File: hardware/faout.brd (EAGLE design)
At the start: 100 x 70 mm, 147 parts, among them IC2 MT48LC8M16A2, Q1 12MHz, Q2 MUN2214T1, Q3 MUN2214T1, Q4 ASFL, SW1 SMD_TACT_SWITCH, SW2 SMD_TACT_SWITCH, SW3 SMD_TACT_SWITCH, U1 93C46B, U10 ADR435ARZ, U11 AD8627AKSZ-R2, U12 OPA2277UA/2K5E4, U13 OPA2277UA/2K5E4, U14 MCP1700T-2502E/TT, U15 AD7980ARMZ, U16 LM3671MF-3.3, U2 LM3671MF-1.2, U3 FLASH-SPI-25XXSMD1, U4 6SLX9TQG144, U5 AD8220ARMZ, U6 REF102AU, U7 DAC8811DGK, U8 REF102AU, U9 DAC8811DGK

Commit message: Finalize design.
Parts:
- removed R30: 7.47k, faout:R0603
- removed R31: 134k, faout:R0603
- removed R32, R33: 2k, faout:R0603
- added C75: 20pF, faout:R0603
- added C76, C77, C80, C81, C82, C83: 100nF, faout:R0603
- added C78, C79: 1nF, faout:R0603
- added C84, C86: 1uF, faout:R0603
- added C85: 22uF, resistor:C1206
- added JP5: (no value), pinhead:1X06
- added Q5: ASFL, crystal:ASF
- added R10, R11, R12: 100, faout:R0603
- added R9: 4.7k, faout:R0603
- added U17: MCP1700T-2502E/TT, faout:SOT95P264X112-3N
- added U18: AD7980ARMZ, faout:SOP50P490X110-10N
- C1: value 3.3uF -> 10uF; device faout:R0603 -> faout:R0805
- C10, C51, C53, C55, C58, C61: value 100nF -> 4.7uF
- C11, C13, C14, C15, C8, C9: value 100nF -> 10uF; device faout:R0603 -> faout:R0805
- C12: value 4.7uF -> 10uF; device faout:R0603 -> faout:R0805
- C17, C25, C26, C27: value 470nF -> 100nF
- C18, C32, C33, C35, C45: value 470nF -> 4.7uF
- C2: value 18pF -> 10uF; device faout:R0603 -> faout:R0805
- C20, C23, C28, C73: value 4.7uF -> 100nF
- C21, C44: value 10nF -> 4.7uF
- C24: value 10nF -> 100nF
- C29, C30, C40, C41, C42, C48: value 4.7uF -> 470nF
- C3: value 18pF -> 3.3uF
- C37, C39: value 470nF -> 10nF
- C38: value 4.7uF -> 100uF; device faout:R0603 -> rcl:PANASONIC_E
- C4: value 4.7uF -> 18pF
- C5: value 100nF -> 18pF
- C50, C62: value 100nF -> 470nF
- C52, C54: value 1uF? -> 470nF
- C56: value 114pF -> 4.7uF
- C57: value 11.4pF -> 4.7uF
- C59: value 20pF -> 10nF
- C60: value 20pF -> 470nF
- C63, C64: value 1nF -> 4.7uF
- C67: value 100nF -> 1uF?
- C69: value 1uF -> 1uF?
- C70: value 22uF -> 100nF; device resistor:C1206 -> faout:R0603
- C71: value 1uF -> 114pF
- C72: value 4.7uF -> 11.4pF
- C74: value 4.7uF -> 20pF
- JP1: device pinhead:1X02 -> pinhead:1X03
- JP2, JP4: device pinhead:1X06 -> pinhead:1X02
- JP3: device pinhead:1X02 -> pinhead:1X06
- Q1: value 12MHz -> L7912ACV; device faout:TXC_QUARTZ_7A -> faout:TO254P450X1020X1935-3P
- Q2: value MUN2214T1 -> 12MHz; device transistor-npn:SC59-BEC -> faout:TXC_QUARTZ_7A
- Q4: value ASFL -> MUN2214T1; device crystal:ASF -> transistor-npn:SC59-BEC
- R13: value 4.7k -> 100
- R17, R18, R19: value 100 -> 10k
- R20: value 100 -> 300
- R21, R22, R23: value 10k -> 300
- R25, R26: value 300 -> 7.47k
- R27: value 300 -> 134k
- R28: value 300 -> 2k
- R29: value 7.47k -> 2k
- U1: value 93C46B -> 93LC46BT-I/OT; device Bogdan_Commons:SOT23-6 -> faout:SOT95P280X145-6N
- U10: value ADR435ARZ -> DAC8811DGK; device faout:SOIC127P600X175-8N -> faout:MSOP-8
- U11: value AD8627AKSZ-R2 -> REF102AU; device faout:SOT65P210X110-5N -> faout:SOIC127P600X175-8N
- U12: value OPA2277UA/2K5E4 -> DAC8811DGK; device faout:SOIC127P600X175-8N -> faout:MSOP-8
- U13: value OPA2277UA/2K5E4 -> ADR435ARZ
- U14: value MCP1700T-2502E/TT -> AD8627AKSZ-R2; device faout:SOT95P264X112-3N -> faout:SOT65P210X110-5N
- U15: value AD7980ARMZ -> OPA2277UA/2K5E4; device faout:SOP50P490X110-10N -> faout:SOIC127P600X175-8N
- U16: value LM3671MF-3.3 -> OPA2277UA/2K5E4; device faout:SOT95P284X122-5N -> faout:SOIC127P600X175-8N
- U2: value LM3671MF-1.2 -> LM3480IM3-3.3; device faout:SOT95P284X122-5N -> faout:SOT95P251X112-3N
- U3: value FLASH-SPI-25XXSMD1 -> LM2940T-12.0; device GadgetFactory:SO08-EIAJ -> faout:TO254P470X1016X2222-3P
- U4: value 6SLX9TQG144 -> LM3671MF-3.3; device faout:TQ144 -> faout:SOT95P284X122-5N
- U5: value AD8220ARMZ -> LM3671MF-1.2; device faout:SOP65P490X110-8N -> faout:SOT95P284X122-5N
- U6: value REF102AU -> FLASH-SPI-25XXSMD1; device faout:SOIC127P600X175-8N -> GadgetFactory:SO08-EIAJ
- U7: value DAC8811DGK -> 6SLX9TQG144; device faout:MSOP-8 -> faout:TQ144
- U8: value REF102AU -> AD8220ARMZ; device faout:SOIC127P600X175-8N -> faout:SOP65P490X110-8N
- U9: value DAC8811DGK -> REF102AU; device faout:MSOP-8 -> faout:SOIC127P600X175-8N
- moved C74 83.9 mm to (87.9, 30.5), turned to 90 degrees
- moved C12 82.6 mm to (87.3, 61.0)
- moved U16 82.4 mm to (83.2, 31.8), turned to 180 degrees
- moved U5 79.4 mm to (6.03, 54.0), turned to 0 degrees
- moved C73 74.5 mm to (81.3, 43.8), turned to 90 degrees
- moved C72 72.2 mm to (79.4, 52.7)
- moved U2 70.3 mm to (75.6, 63.5), turned to 90 degrees
- moved JP4 64.2 mm to (6.35, 19.4), turned to 180 degrees
- moved JP1 63.5 mm to (95.9, 64.1), turned to 90 degrees
- moved JP3 62.3 mm to (55.9, 57.1), turned to 90 degrees
- moved Q2 60.1 mm to (34.9, 62.5), turned to 180 degrees
- moved U3 57.9 mm to (85.7, 64.8), turned to 0 degrees
- moved C32 56.2 mm to (7.94, 64.5), flipped to the top, turned to 180 degrees
- moved C35 53.2 mm to (7.94, 65.7), flipped to the top
- moved Q4 52.8 mm to (22.5, 2.86), flipped to the top, turned to 90 degrees
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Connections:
- new net +15V: C1.1, JP1.1, U2.2, U3.1
- new net -15V: C2.1, JP1.2, Q1.2
- net !DAC1_CS: now also U10.8, U7.94; no longer U4.94, U7.8
- net !DAC2_CS: now also U12.8, U7.88; no longer U4.88, U9.8
- net !RAM_CAS: now also U7.5; no longer U4.5
- net !RAM_RAS: now also U7.2; no longer U4.2
- net !RAM_WE: now also U7.6; no longer U4.6
- net !USB_OE: now also U7.116; no longer U4.116
- net !USB_RD: now also U7.119; no longer U4.119
- net !USB_RESET: now also JP2.1; no longer JP1.1
- net !USB_RXF: now also U7.121; no longer U4.121
- net !USB_TXE: now also U7.120; no longer U4.120
- net !USB_WR: now also U7.118; no longer U4.118
- net 1V2: now also C33.1, C36.1, C41.1, C43.1, C45.1, C46.1, U5.4, U7.128, U7.19, U7.28, U7.52, U7.89; no longer C26.1, C28.1, C30.1, C31.1, C73.1, C74.1, U2.4, U4.128, U4.19, U4.28, U4.52, U4.89
- net 1V8: now also C20.1, C23.1, C24.1, C3.1; no longer C1.1, C10.1, C11.1, C9.1
- net 2V5: now also C84.1, U17.2, U18.2; no longer C69.1, U14.2, U15.2
- net 3V3: now also C26.1, C28.1, C30.1, C31.1, C38.+, C50.1, C51.1, C52.1, C53.1, C54.1, C55.1, C56.1, C57.1, C58.1, C59.1, C60.1, C61.1, C62.1, C63.1, C64.1, C7.1, JP3.6, JP5.6, Q5.1, Q5.4, R17.2, R18.2, R19.2, R9.2, U5.3, U6.3, U6.7, U6.8, U7.103, U7.122, U7.125, U7.129, U7.135, U7.18, U7.20, U7.31, U7.36, U7.4, U7.42, U7.53, U7.63, U7.69, U7.76, U7.86, U7.90; no longer C13.1, C14.1, C15.1, C16.1, C17.1, C18.1, C19.1, C20.1, C21.1, C23.1, C24.1, C33.1, C36.1, C38.1, C41.1, C43.1, C45.1, C46.1, C5.1, C72.1, JP2.6, JP4.6, Q4.1, Q4.4, R13.2, R21.2, R22.2, R23.2, U16.4, U2.3, U3.3, U3.7, U3.8, U4.103, U4.122, U4.125, U4.129, U4.135, U4.18, U4.20, U4.31, U4.36, U4.42, U4.53, U4.63, U4.69, U4.76, U4.86, U4.90
- net 5V0: now also C18.1, C19.1, C21.1, U4.1, U4.3, U5.1; no longer C12.1, U16.1, U16.3, U2.1
- net A+12V: now also C12.1, C14.1, C73.1, C76.1, C8.1, C80.1, C82.1, U13.2, U14.5, U15.8, U16.8, U3.3, U8.8; no longer C50.1, C58.1, C61.1, C67.1, U10.2, U11.5, U12.8, U13.8, U5.8
- net A+3V3: now also C11.1, C67.1, C68.1, C69.1, C70.1, C86.1, U10.7, U11.2, U12.7, U17.3, U18.10, U2.1, U9.2; no longer C52.1, C53.1, C54.1, C55.1, C71.1, U14.3, U15.10, U6.2, U7.7, U8.2, U9.7
- net A-12V: now also C13.2, C15.2, C77.2, C81.2, C83.2, C9.2, Q1.3, U14.2, U15.4, U16.4, U8.5; no longer C51.2, C62.2, C68.2, U11.2, U12.4, U13.4, U5.5
- net ADC1_CNV: now also U18.6, U7.100; no longer U15.6, U4.100
- net ADC1_REF: now also C85.1, U13.6, U18.1; no longer C70.1, U10.6, U15.1
- net ADC1_SCK: now also U18.8, U7.98; no longer U15.8, U4.98
- net ADC1_SDI: now also U18.9, U7.97; no longer U15.9, U4.97
- net ADC1_SDO: now also U18.7, U7.99; no longer U15.7, U4.99
- net BUTTON1: now also U7.61; no longer U4.61
- net BUTTON2: now also U7.62; no longer U4.62
- net BUTTON3: now also U7.66; no longer U4.66
- net CLK_IN: now also Q5.3, U7.95; no longer Q4.3, U4.95
- net DAC1_CLK: now also U10.1, U7.93; no longer U4.93, U7.1
- net DAC1_IOUT: now also C74.2, U10.5, U16.2; no longer C59.2, U13.2, U7.5
- net DAC1_SDI: now also U10.2, U7.92; no longer U4.92, U7.2
- net DAC1_VOUT: now also C74.1, U10.3, U16.1; no longer C59.1, U13.1, U7.3
- net DAC1_VREF: now also C67.2, C78.2, U10.4, U16.7, U9.4; no longer C52.2, C63.2, U13.7, U6.4, U7.4
- net DAC1_VREFOUT: now also C78.1, R28.2, U16.6; no longer C63.1, R32.2, U13.6
- net DAC2_CLK: now also U12.1, U7.87; no longer U4.87, U9.1
- net DAC2_IOUT: now also C75.2, U12.5, U15.2; no longer C60.2, U12.2, U9.5
- net DAC2_SDI: now also U12.2, U7.85; no longer U4.85, U9.2
- net DAC2_VOUT: now also C75.1, U12.3, U15.1; no longer C60.1, U12.1, U9.3
- net DAC2_VREF: now also C69.2, C79.2, U11.4, U12.4, U15.7; no longer C54.2, C64.2, U12.7, U8.4, U9.4
- net DAC2_VREFOUT: now also C79.1, R29.2, U15.6; no longer C64.1, R33.2, U12.6
- net DISP_A: now also R10.2, U7.55; no longer R14.2, U4.55
- net DISP_B: now also R11.2, U7.56; no longer R15.2, U4.56
- net DISP_C: now also R12.2, U7.48; no longer R16.2, U4.48
- net DISP_CAT1: now also Q4.C; no longer Q3.C
- net DISP_D: now also R13.2, U7.50; no longer R17.2, U4.50
- net DISP_E: now also R14.2, U7.47; no longer R18.2, U4.47
- net DISP_EN1: now also Q4.B, U7.58; no longer Q3.B, U4.58
- net DISP_EN2: now also Q3.B, U7.59; no longer Q2.B, U4.59
- net DISP_F: now also R15.2, U7.51; no longer R19.2, U4.51
- net DISP_G: now also R16.2, U7.57; no longer R20.2, U4.57
- net DISP_INT_A: now also R10.1; no longer R14.1
- net DISP_INT_B: now also R11.1; no longer R15.1
- net DISP_INT_C: now also R12.1; no longer R16.1
- net DISP_INT_D: now also R13.1; no longer R17.1
- net DISP_INT_E: now also R14.1; no longer R18.1
- net DISP_INT_F: now also R15.1; no longer R19.1
- net DISP_INT_G: now also R16.1; no longer R20.1
- net FLASH_CS: now also U6.1, U7.38; no longer U3.1, U4.38
- net FLASH_MISO: now also U6.2, U7.65; no longer U3.2, U4.65
- net FLASH_MOSI: now also U6.5, U7.64; no longer U3.5, U4.64
- net FLASH_SCK: now also U6.6, U7.70; no longer U3.6, U4.70
- net GND: now also C13.1, C15.1, C38.-, C51.2, C52.2, C54.2, C56.2, C59.2, C60.2, C62.2, C63.2, C64.2, C68.2, C76.2, C77.1, C80.2, C81.1, C82.2, C83.1, C84.2, C85.2, C86.2, C9.1, JP1.3, JP2.2, JP3.1, JP4.2, JP5.5, Q1.1, Q4.E, Q5.2, R20.1, R21.1, R22.1, R23.1, U10.6, U12.6, U13.4, U15.3, U16.3, U16.5, U17.1, U18.4, U18.5, U2.3, U3.2, U4.2, U5.2, U6.4, U7.108, U7.113, U7.13, U7.130, U7.136, U7.144, U7.25, U7.3, U7.49, U7.54, U7.60, U7.68, U7.73, U7.77, U7.91, U7.96, U8.6; no longer C13.2, C15.2, C38.2, C51.1, C62.1, C67.2, C68.1, C69.2, C71.2, C74.2, C9.2, JP1.2, JP2.1, JP3.2, JP4.5, Q2.E, Q4.2, R25.1, R27.1, R28.1, R30.1, U10.4, U12.3, U12.5, U13.3, U13.5, U14.1, U15.4, U16.2, U2.2, U3.4, U4.108, U4.113, U4.13, U4.130, U4.136, U4.144, U4.25, U4.3, U4.49, U4.54, U4.60, U4.68, U4.73, U4.77, U4.91, U4.96, U5.6, U7.6, U9.6
- net JP_1: now also JP5.1, U7.84; no longer JP4.1, U4.84
- net JP_2: now also JP5.2, U7.83; no longer JP4.2, U4.83
- net JP_3: now also JP5.3, U7.82; no longer JP4.3, U4.82
- net JP_4: now also JP5.4, U7.81; no longer JP4.4, U4.81
- net LED1: now also U7.80; no longer U4.80
- net LED2: now also U7.79; no longer U4.79
- net LED3: now also U7.78; no longer U4.78
- net LED_4: now also U7.112; no longer U4.112
- net LED_5: now also U7.111; no longer U4.111
- net N$1: now also C4.1, Q2.1; no longer C2.1, Q1.1
- net N$10: now also R28.1, U9.6; no longer R32.1, U6.6
- net N$11: now also U8.1; no longer U5.1
- net N$12: now also C71.1, U14.1, U14.4, U18.3; no longer C56.1, U11.1, U11.4, U15.3
- net N$13: now also R25.2, U8.7; no longer R29.2, U5.7
- net N$14: now also C71.2, R25.1, R26.2, R27.1; no longer C56.2, R29.1, R30.2, R31.1
- net N$15: now also C72.1, R27.2, U14.3; no longer C57.1, R31.2, U11.3
- net N$17: now also Q3.C; no longer Q2.C
- net N$18: now also R17.1; no longer R21.1
- net N$19: now also R18.1; no longer R22.1
- net N$2: now also C5.1, Q2.2; no longer C3.1, Q1.2
- net N$20: now also R19.1; no longer R23.1
- net N$21: now also R20.2; no longer R24.2
- net N$22: now also R21.2; no longer R25.2
- net N$23: now also R22.2; no longer R26.2
- net N$24: now also U4.5; no longer U16.5
- net N$25: now also U5.5; no longer U2.5
- net N$3: now also R23.2; no longer R27.2
- net N$4: now also R24.2; no longer R28.2
- net N$5: now also C16.1, C6.1; no longer C4.1, C7.1
- net N$7: now also C10.1, C17.1; no longer C6.1, C8.1
- net N$8: now also R29.1, U11.6; no longer R33.1, U8.6
- net N$9: now also U8.4; no longer U5.4
- net RAM_A0: now also U7.140; no longer U4.140
- net RAM_A1: now also U7.139; no longer U4.139
- net RAM_A10: now also U7.141; no longer U4.141
- net RAM_A11: now also U7.35; no longer U4.35
- net RAM_A2: now also U7.138; no longer U4.138
- net RAM_A3: now also U7.137; no longer U4.137
- net RAM_A4: now also U7.46; no longer U4.46
- net RAM_A5: now also U7.45; no longer U4.45
- net RAM_A6: now also U7.44; no longer U4.44
- net RAM_A7: now also U7.43; no longer U4.43
- net RAM_A8: now also U7.41; no longer U4.41
- net RAM_A9: now also U7.40; no longer U4.40
- net RAM_BA0: now also U7.143; no longer U4.143
- net RAM_BA1: now also U7.142; no longer U4.142
- net RAM_CKE: now also U7.33; no longer U4.33
- net RAM_CLK: now also U7.32; no longer U4.32
- net RAM_CS: now also U7.1; no longer U4.1
- net RAM_DQ0: now also U7.9; no longer U4.9
- net RAM_DQ1: now also U7.10; no longer U4.10
- net RAM_DQ10: now also U7.23; no longer U4.23
- net RAM_DQ11: now also U7.24; no longer U4.24
- net RAM_DQ12: now also U7.26; no longer U4.26
- net RAM_DQ13: now also U7.27; no longer U4.27
- net RAM_DQ14: now also U7.29; no longer U4.29
- net RAM_DQ15: now also U7.30; no longer U4.30
- net RAM_DQ2: now also U7.11; no longer U4.11
- net RAM_DQ3: now also U7.12; no longer U4.12
- net RAM_DQ4: now also U7.14; no longer U4.14
- net RAM_DQ5: now also U7.15; no longer U4.15
- net RAM_DQ6: now also U7.16; no longer U4.16
- net RAM_DQ7: now also U7.8; no longer U4.8
- net RAM_DQ8: now also U7.21; no longer U4.21
- net RAM_DQ9: now also U7.22; no longer U4.22
- net RAM_DQMH: now also U7.17; no longer U4.17
- net RAM_DQML: now also U7.7; no longer U4.7
- net RESET: now also JP4.1, R9.1, U7.37; no longer JP3.1, R13.1, U4.37
- net TCK: now also JP3.2, U7.109; no longer JP2.2, U4.109
- net TDI: now also JP3.3, U7.110; no longer JP2.3, U4.110
- net TDO: now also JP3.4, U7.106; no longer JP2.4, U4.106
- net TMS: now also JP3.5, U7.107; no longer JP2.5, U4.107
- net USB_CLKOUT: now also U7.123; no longer U4.123
- net USB_D0: now also U7.117; no longer U4.117
- net USB_D1: now also U7.134; no longer U4.134
- net USB_D2: now also U7.133; no longer U4.133
- net USB_D3: now also U7.132; no longer U4.132
- net USB_D4: now also U7.131; no longer U4.131
- net USB_D5: now also U7.127; no longer U4.127
- net USB_D6: now also U7.126; no longer U4.126
- net USB_D7: now also U7.124; no longer U4.124
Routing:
- net 3V3: track 381.6 -> 448.7 mm, vias 38 -> 53
- net 1V2: track 47.0 -> 94.8 mm, vias 5 -> 11
- net USB_V: track 69.8 -> 26.8 mm
- net -15V: track 0.00 -> 36.0 mm
- net +15V: track 0.00 -> 26.0 mm
- net USB_GND: track 26.2 -> 7.79 mm
- net A+3V3: track 121.7 -> 136.4 mm, vias 8 -> 10
- net A-12V: track 85.9 -> 99.8 mm
- net GND: track 6.00 -> 3.14 mm, vias 178 -> 241
- net ADC1_SDI: track 26.2 -> 23.7 mm
- net ADC1_SDO: track 26.2 -> 23.7 mm
- net ADC1_CNV: track 26.2 -> 23.7 mm
- net ADC1_SCK: track 26.2 -> 23.7 mm
- net N$24: track 0.00 -> 2.38 mm
- net N$25: track 0.00 -> 2.38 mm
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- removed copper zone on layer 1, net N$26
- removed copper zone on layer 16, net N$26

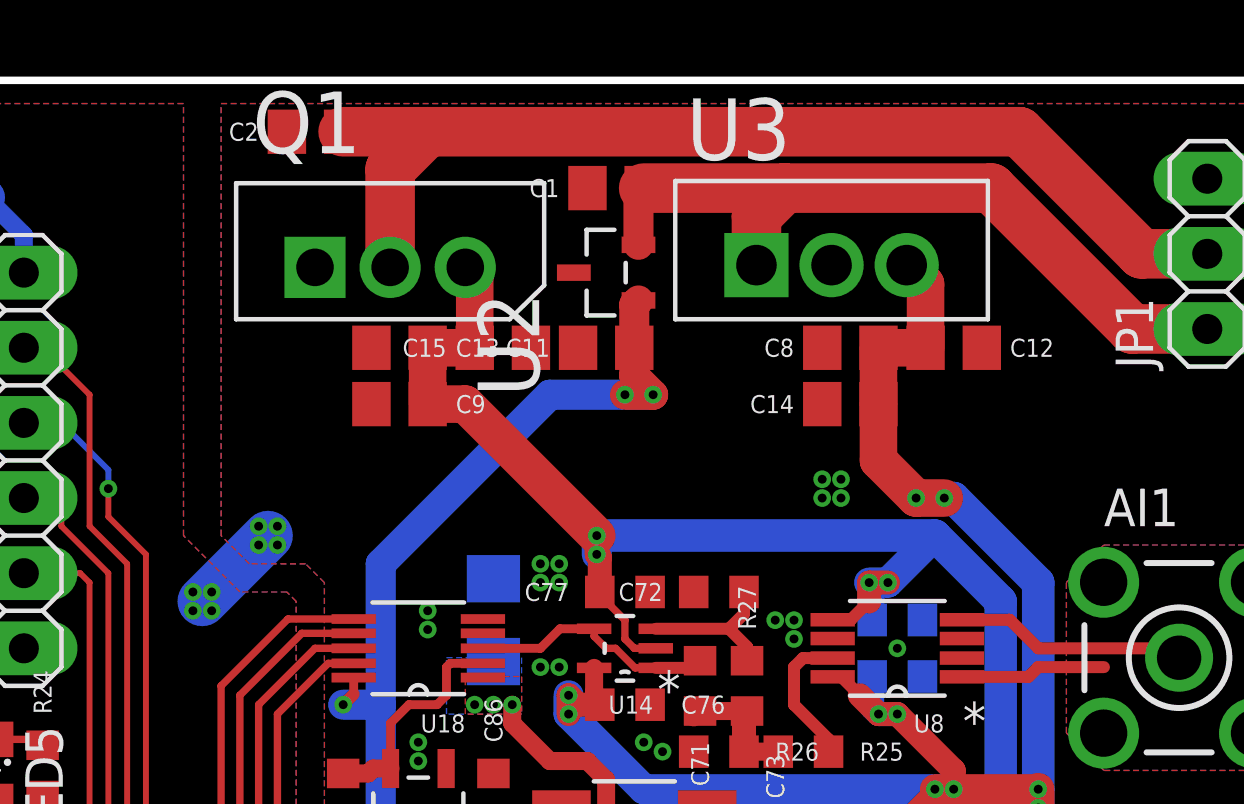
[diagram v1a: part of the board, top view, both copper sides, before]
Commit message: Unify analog regulators.
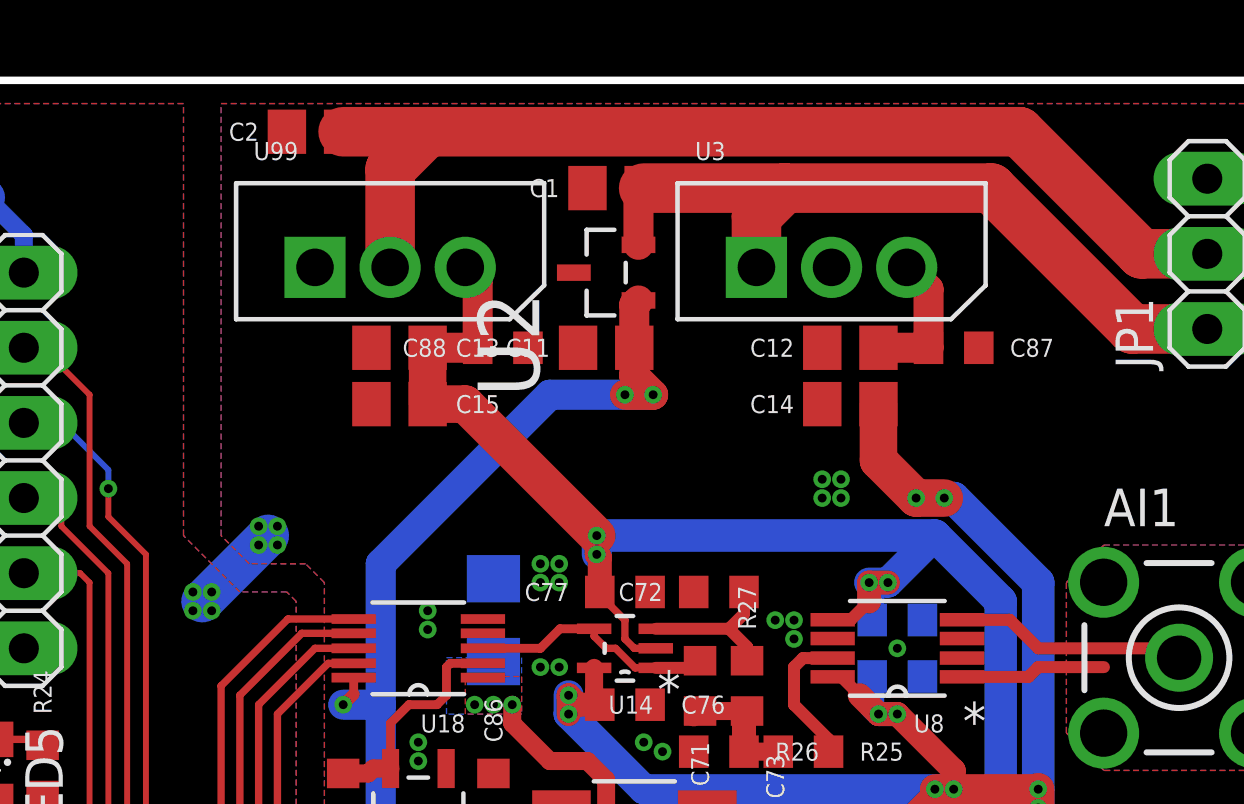
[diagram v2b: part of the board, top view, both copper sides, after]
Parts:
- removed C8, C9: 10uF, faout:R0805
- added C87, C88: 100nF, faout:R0603
- U3: value LM2940T-12.0 -> L7812ACV; device faout:TO254P470X1016X2222-3P -> faout:TO254P450X1020X1935-3P
- moved C15 3.98 mm to (68.6, 59.1), turned to 0 degrees
- moved C12 3.49 mm to (83.8, 61.0), turned to 180 degrees
- renumbered Q1 to U99
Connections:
- net A+12V: now also C87.1; no longer C8.1
- net A-12V: now also C88.2; no longer C9.2
- net GND: now also C87.2, C88.1; no longer C8.2, C9.1
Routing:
- net A+12V: track 123.9 -> 122.1 mm
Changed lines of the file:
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@@
 </element>
 <element name="JP1" library="pinhead" package="1X03" value="" x="95.885" y="64.135" rot="R90"/>
-<element name="U3" library="faout" package="TO254P470X1016X2222-3P" value="LM2940T-12.0" x="85.725" y="64.77">
+<element name="U3" library="faout" package="TO254P450X1020X1935-3P" value="L7812ACV" x="85.725" y="64.77">
 <attribute name="PACKAGE" value="TO-220" x="85.725" y="64.77" size="1.778" layer="27" display="off"/>
-<attribute name="OC_NEWARK" value="41K4614" x="85.725" y="64.77" size="1.778" layer="27" display="off"/>
-<attribute name="MPN" value="LM2940T-12.0" x="85.725" y="64.77" size="1.778" layer="27" display="off"/>
-<attribute name="SUPPLIER" value="NATIONAL SEMICONDUCTOR" x="85.725" y="64.77" size="1.778" layer="27" display="off"/>
-<attribute name="OC_FARNELL" value="9485872" x="85.725" y="64.77" size="1.778" layer="27" display="off"/>
+<attribute name="OC_NEWARK" value="89K0786" x="85.725" y="64.77" size="1.778" layer="27" display="off"/>
+<attribute name="MPN" value="L7812ACV" x="85.725" y="64.77" size="1.778" layer="27" display="off"/>
+<attribute name="SUPPLIER" value="STMicroelectronics" x="85.725" y="64.77" size="1.778" layer="27" display="off"/>
+<attribute name="OC_FARNELL" value="1087091" x="85.725" y="64.77" size="1.778" layer="27" display="off"/>
 </element>
-<element name="Q1" library="faout" package="TO254P450X1020X1935-3P" value="L7912ACV" x="70.8025" y="64.77">
+<element name="U99" library="faout" package="TO254P450X1020X1935-3P" value="L7912ACV" x="70.8025" y="64.77">
 <attribute name="PACKAGE" value="TO-220" x="70.8025" y="64.77" size="1.778" layer="27" display="off"/>
 <attribute name="OC_NEWARK" value="89K0792" x="70.8025" y="64.77" size="1.778" layer="27" display="off"/>
@@
 <attribute name="OC_FARNELL" value="1095391" x="70.8025" y="64.77" size="1.778" layer="27" display="off"/>
 </element>
-<element name="C12" library="faout" package="R0805" value="10uF" x="87.3125" y="60.96">
-<attribute name="OC_FARNELL" value="1867958" x="87.3125" y="60.96" size="1.778" layer="27" display="off"/>
-</element>
-<element name="C8" library="faout" package="R0805" value="10uF" x="83.82" y="60.96" rot="R180">
+<element name="C12" library="faout" package="R0805" value="10uF" x="83.82" y="60.96" rot="R180">
 <attribute name="OC_FARNELL" value="1867958" x="83.82" y="60.96" size="1.778" layer="27" rot="R180" display="off"/>
 </element>
@@
 <attribute name="OC_FARNELL" value="1867958" x="83.82" y="59.055" size="1.778" layer="27" rot="R180" display="off"/>
 </element>
-<element name="C9" library="faout" package="R0805" value="10uF" x="68.58" y="59.055">
-<attribute name="OC_FARNELL" value="1867958" x="68.58" y="59.055" size="1.778" layer="27" display="off"/>
-</element>
 <element name="C13" library="faout" package="R0805" value="10uF" x="68.58" y="60.96">
 <attribute name="OC_FARNELL" value="1867958" x="68.58" y="60.96" size="1.778" layer="27" display="off"/>
 </element>
-<element name="C15" library="faout" package="R0805" value="10uF" x="72.0725" y="60.96" rot="R180">
-<attribute name="OC_FARNELL" value="1867958" x="72.0725" y="60.96" size="1.778" layer="27" rot="R180" display="off"/>
+<element name="C15" library="faout" package="R0805" value="10uF" x="68.58" y="59.055">
+<attribute name="OC_FARNELL" value="1867958" x="68.58" y="59.055" size="1.778" layer="27" display="off"/>
 </element>
 <element name="C1" library="faout" package="R0805" value="10uF" x="75.8825" y="66.3575" rot="R180">
@@
 <attribute name="SUPPLIER" value="Microchip" x="41.5925" y="66.3575" size="1.778" layer="27" display="off"/>
 <attribute name="OC_FARNELL" value="1556164" x="41.5925" y="66.3575" size="1.778" layer="27" display="off"/>
+</element>
+<element name="C87" library="faout" package="R0603" value="100nF" x="87.3125" y="60.96">
+<attribute name="OC_FARNELL" value="1740621" x="87.3125" y="60.96" size="1.778" layer="27" display="off"/>
+</element>
+<element name="C88" library="faout" package="R0603" value="100nF" x="72.0725" y="60.96" rot="R180">
+<attribute name="OC_FARNELL" value="1740621" x="72.0725" y="60.96" size="1.778" layer="27" rot="R180" display="off"/>
 </element>
 </elements>
@@
 <vertex x="62.5475" y="54.61"/>
 </polygon>
-<wire x1="61.9125" y1="52.3875" x2="64.135" y2="54.61" width="1.6764" layer="16"/>
+<wire x1="61.9125" y1="52.3875" x2="64.135" y2="54.61" width="1.4224" layer="16"/>
 <polygon width="0.25" layer="16" rank="6">
 <vertex x="62.5475" y="69.215"/>
@@
 <via x="19.3675" y="35.8775" extent="1-16" drill="0.3"/>
 <contactref element="JP1" pad="3"/>
-<contactref element="Q1" pad="1"/>
+<contactref element="U99" pad="1"/>
 <contactref element="U3" pad="2"/>
 <contactref element="C1" pad="2"/>
 <contactref element="C2" pad="2"/>
-<contactref element="C9" pad="1"/>
-<contactref element="C8" pad="2"/>
 <contactref element="C14" pad="2"/>
 <contactref element="C12" pad="2"/>
@@
 <via x="49.8475" y="67.945" extent="1-16" drill="0.3"/>
 <via x="50.4825" y="67.945" extent="1-16" drill="0.3"/>
+<contactref element="C88" pad="1"/>
+<contactref element="C87" pad="2"/>
 </signal>
 <signal name="USB_DM">
@@
 <contactref element="U3" pad="3"/>
 <contactref element="C12" pad="1"/>
-<contactref element="C8" pad="1"/>
 <contactref element="C14" pad="1"/>
-<wire x1="86.3625" y1="60.96" x2="84.77" y2="60.96" width="1.27" layer="1"/>
-<wire x1="84.77" y1="59.055" x2="84.77" y2="60.96" width="1.27" layer="1"/>
-<wire x1="86.3625" y1="60.96" x2="86.3625" y2="63.1165" width="1.27" layer="1"/>
-<wire x1="86.3625" y1="63.1165" x2="85.725" y2="63.754" width="1.27" layer="1"/>
 <wire x1="84.77" y1="59.055" x2="84.77" y2="57.1525" width="1.27" layer="1"/>
 <wire x1="84.77" y1="57.1525" x2="86.0425" y2="55.88" width="1.27" layer="1"/>
@@
 <via x="86.0425" y="55.88" extent="1-16" drill="0.3"/>
 <via x="86.995" y="55.88" extent="1-16" drill="0.3"/>
+<contactref element="C87" pad="1"/>
+<wire x1="86.4625" y1="60.96" x2="86.4625" y2="62.9403" width="1.016" layer="1"/>
+<wire x1="86.4625" y1="62.9403" x2="85.725" y2="63.6778" width="1.016" layer="1"/>
+<wire x1="86.4625" y1="60.96" x2="84.77" y2="60.96" width="1.016" layer="1"/>
+<wire x1="84.77" y1="59.055" x2="84.77" y2="60.96" width="0" layer="19" extent="1-1"/>
 </signal>
 <signal name="A+3V3">
@@
 <via x="75.2475" y="53.975" extent="1-16" drill="0.3"/>
 <wire x1="75.2475" y1="54.61" x2="75.2475" y2="53.975" width="1.016" layer="16"/>
-<contactref element="Q1" pad="3"/>
-<contactref element="C9" pad="2"/>
 <contactref element="C13" pad="2"/>
 <contactref element="C15" pad="2"/>
+<wire x1="70.8025" y1="59.055" x2="75.2475" y2="54.61" width="1.27" layer="1"/>
+<contactref element="U99" pad="3"/>
+<contactref element="C88" pad="2"/>
+<wire x1="71.2225" y1="60.96" x2="71.2225" y2="63.2578" width="1.016" layer="1"/>
+<wire x1="71.2225" y1="63.2578" x2="70.8025" y2="63.6778" width="1.016" layer="1"/>
+<wire x1="71.2225" y1="60.96" x2="69.53" y2="60.96" width="1.016" layer="1"/>
+<wire x1="70.8025" y1="59.055" x2="69.53" y2="59.055" width="1.27" layer="1"/>
 <wire x1="69.53" y1="59.055" x2="69.53" y2="60.96" width="1.27" layer="1"/>
-<wire x1="69.53" y1="60.96" x2="71.1225" y2="60.96" width="1.27" layer="1"/>
-<wire x1="71.1225" y1="60.96" x2="71.1225" y2="63.3578" width="1.27" layer="1"/>
-<wire x1="71.1225" y1="63.3578" x2="70.8025" y2="63.6778" width="1.27" layer="1"/>
-<wire x1="69.53" y1="59.055" x2="70.8025" y2="59.055" width="1.27" layer="1"/>
-<wire x1="70.8025" y1="59.055" x2="75.2475" y2="54.61" width="1.27" layer="1"/>
 </signal>
 <signal name="N$12">
@@
 <contactref element="JP1" pad="1"/>
 <contactref element="U3" pad="1"/>
-<wire x1="80.645" y1="63.754" x2="80.645" y2="65.405" width="1.6764" layer="1"/>
+<wire x1="80.645" y1="63.6778" x2="80.645" y2="65.405" width="1.6764" layer="1"/>
 <wire x1="80.645" y1="65.405" x2="81.5975" y2="66.3575" width="1.6764" layer="1"/>
 <wire x1="81.5975" y1="66.3575" x2="88.5825" y2="66.3575" width="1.6764" layer="1"/>
@@
 <signal name="-15V">
 <contactref element="JP1" pad="2"/>
-<contactref element="Q1" pad="2"/>
+<contactref element="U99" pad="2"/>
 <wire x1="95.885" y1="64.135" x2="93.6625" y2="64.135" width="1.6764" layer="1"/>
 <wire x1="93.6625" y1="64.135" x2="89.535" y2="68.2625" width="1.6764" layer="1"/>
